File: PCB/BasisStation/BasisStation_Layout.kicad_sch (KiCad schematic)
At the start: 18 parts, among them J5 Conn_02x05_Odd_Even, J6 Conn_02x03_Odd_Even, U6 ESP32-S3-WROOM-1

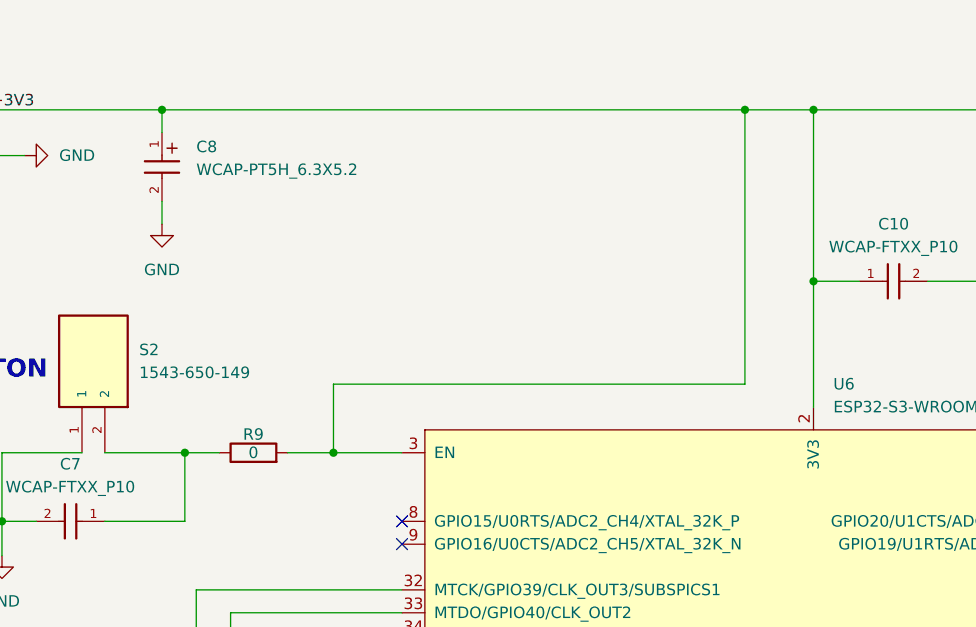
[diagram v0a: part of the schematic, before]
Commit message: Widerstand versetzt
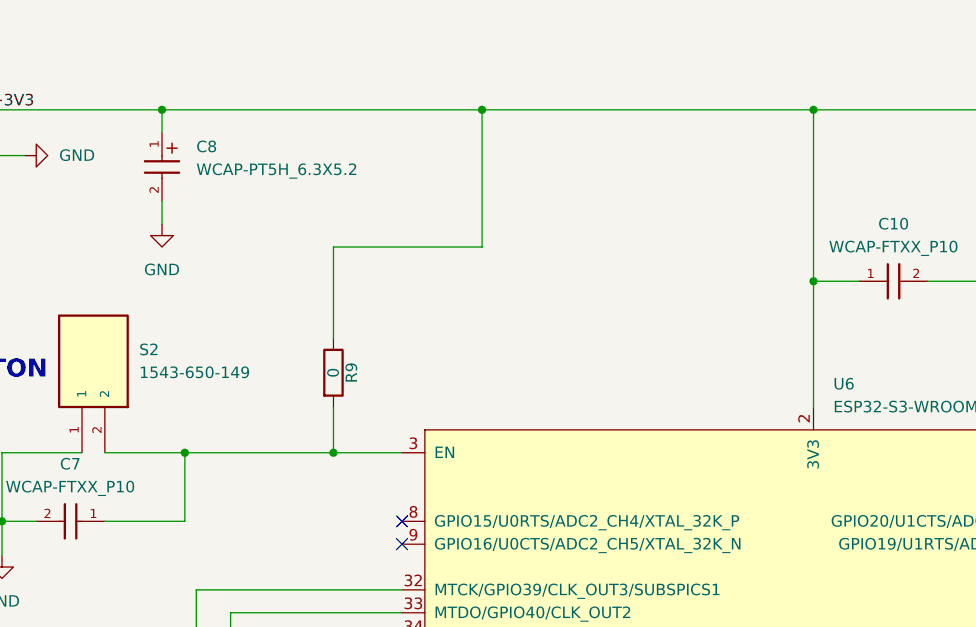
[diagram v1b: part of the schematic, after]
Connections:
- net +3V3: now also R9.1; no longer R9.2, U6.3 (EN)
- net at C7.1, S2.2: now also R9.2, U6.3 (EN); no longer R9.1
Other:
- moved on the sheet: R9

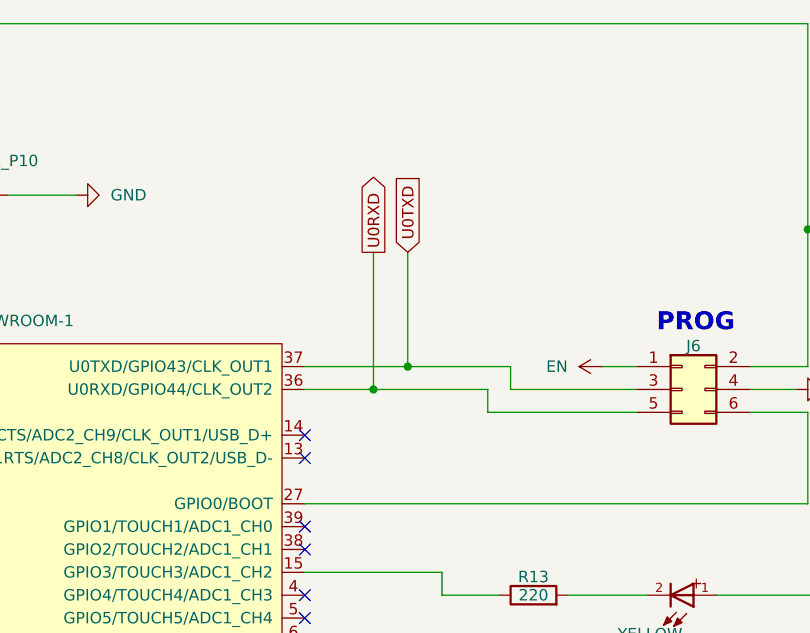
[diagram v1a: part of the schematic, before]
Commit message: USB-Bridge entfernt. Globale Bezeichner USB+ und USB- hinzugefügt
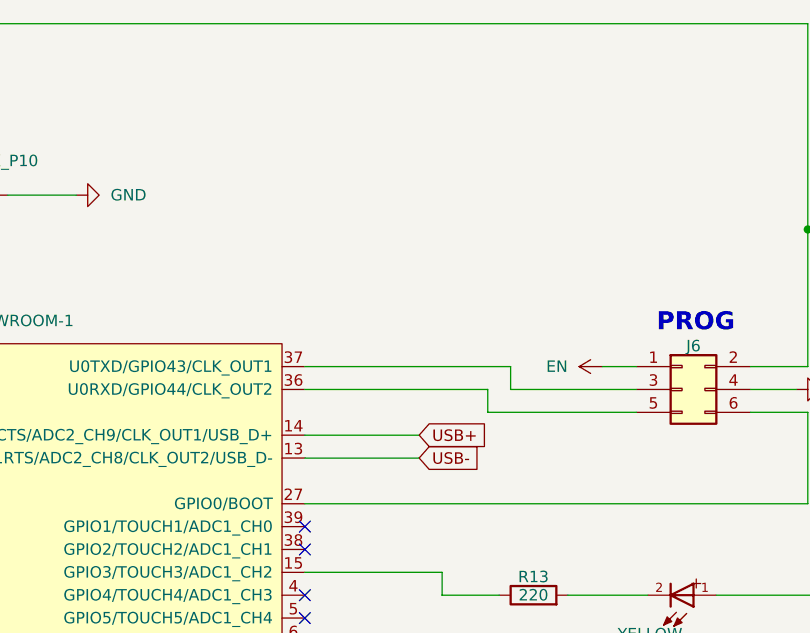
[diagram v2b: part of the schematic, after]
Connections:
- net USB-: now reaches U6.13 (GPIO19/U1RTS/ADC2_CH8/CLK_OUT2/USB_D-)
- net USB+: now reaches U6.14 (GPIO20/U1CTS/ADC2_CH9/CLK_OUT1/USB_D+)
- net U0RXD: no longer names the net of J6.5 (Pin_5), U6.36 (U0RXD/GPIO44/CLK_OUT2)
- net U0TXD: no longer names the net of J6.3 (Pin_3), U6.37 (U0TXD/GPIO43/CLK_OUT1)
- no-connect marks 26 -> 24
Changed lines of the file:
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@@
-	)
-	(junction
-		(at 195.58 60.96)
-		(diameter 0)
-		(color 0 0 0 0)
 	)
 	(junction
@@
 	)
 	(junction
-		(at 191.77 63.5)
-		(diameter 0)
-		(color 0 0 0 0)
-	)
-	(junction
 		(at 68.58 60.96)
 		(diameter 0)
@@
 	)
 	(no_connect
-		(at 184.15 68.58)
-	)
-	(no_connect
 		(at 92.71 127)
 	)
@@
 	)
 	(no_connect
-		(at 184.15 71.12)
-	)
-	(no_connect
 		(at 184.15 129.54)
 	)
@@
 	(wire
 		(pts
-			(xy 191.77 48.26) (xy 191.77 63.5)
-		)
-		(stroke
-			(width 0)
-			(type default)
-		)
-	)
-	(wire
-		(pts
 			(xy 48.26 68.58) (xy 52.07 68.58)
 		)
@@
 	(wire
 		(pts
-			(xy 195.58 48.26) (xy 195.58 60.96)
-		)
-		(stroke
-			(width 0)
-			(type default)
-		)
-	)
-	(wire
-		(pts
 			(xy 195.58 127) (xy 184.15 127)
 		)
@@
 	(wire
 		(pts
+			(xy 184.15 71.12) (xy 196.85 71.12)
+		)
+		(stroke
+			(width 0)
+			(type default)
+		)
+	)
+	(wire
+		(pts
 			(xy 213.36 104.14) (xy 222.25 104.14)
 		)
@@
 	(wire
 		(pts
-			(xy 191.77 63.5) (xy 204.47 63.5)
+			(xy 184.15 63.5) (xy 204.47 63.5)
 		)
 		(stroke
@@
 	(wire
 		(pts
+			(xy 184.15 68.58) (xy 196.85 68.58)
+		)
+		(stroke
+			(width 0)
+			(type default)
+		)
+	)
+	(wire
+		(pts
 			(xy 41.91 186.69) (xy 41.91 190.5)
 		)
@@
 	(wire
 		(pts
-			(xy 184.15 60.96) (xy 195.58 60.96)
+			(xy 184.15 60.96) (xy 207.01 60.96)
 		)
 		(stroke
@@
 	(wire
 		(pts
-			(xy 195.58 60.96) (xy 207.01 60.96)
-		)
-		(stroke
-			(width 0)
-			(type default)
-		)
-	)
-	(wire
-		(pts
 			(xy 68.58 68.58) (xy 68.58 60.96)
 		)
@@
 		(pts
 			(xy 199.39 83.82) (xy 184.15 83.82)
-		)
-		(stroke
-			(width 0)
-			(type default)
-		)
-	)
-	(wire
-		(pts
-			(xy 184.15 63.5) (xy 191.77 63.5)
 		)
 		(stroke
@@
 		)
 	)
-	(global_label "U0TXD"
+	(global_label "USB-"
 		(shape input)
-		(at 195.58 48.26 90)
+		(at 196.85 71.12 0)
 		(fields_autoplaced yes)
 		(effects
@@
 		)
 		(property "Intersheetrefs" "${INTERSHEET_REFS}"
-			(at 195.58 39.2877 90)
+			(at 205.2176 71.12 0)
 			(effects
 				(font
@@
 		)
 	)
-	(global_label "U0RXD"
-		(shape output)
-		(at 191.77 48.26 90)
+	(global_label "USB+"
+		(shape input)
+		(at 196.85 68.58 0)
 		(fields_autoplaced yes)
 		(effects
@@
 		)
 		(property "Intersheetrefs" "${INTERSHEET_REFS}"
-			(at 191.77 38.9853 90)
+			(at 205.2176 68.58 0)
 			(effects
 				(font

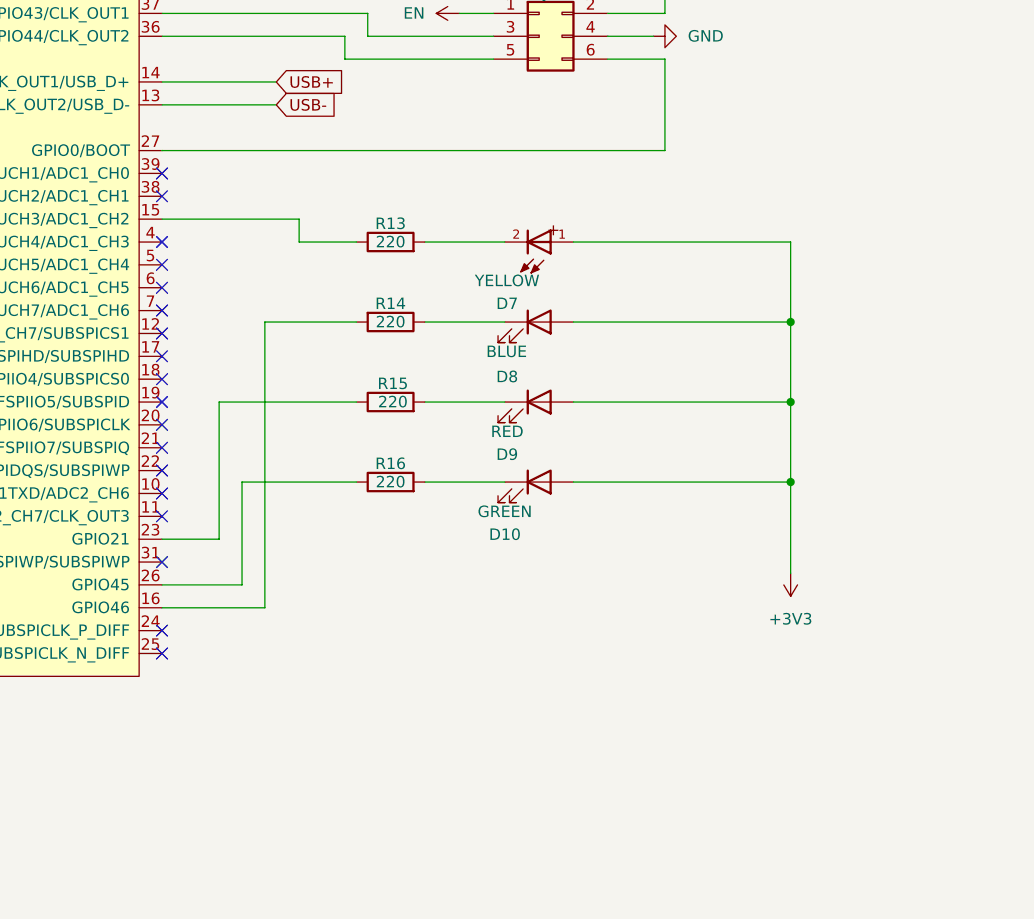
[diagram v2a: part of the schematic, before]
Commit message: Steuerund der LEDs umgebaut
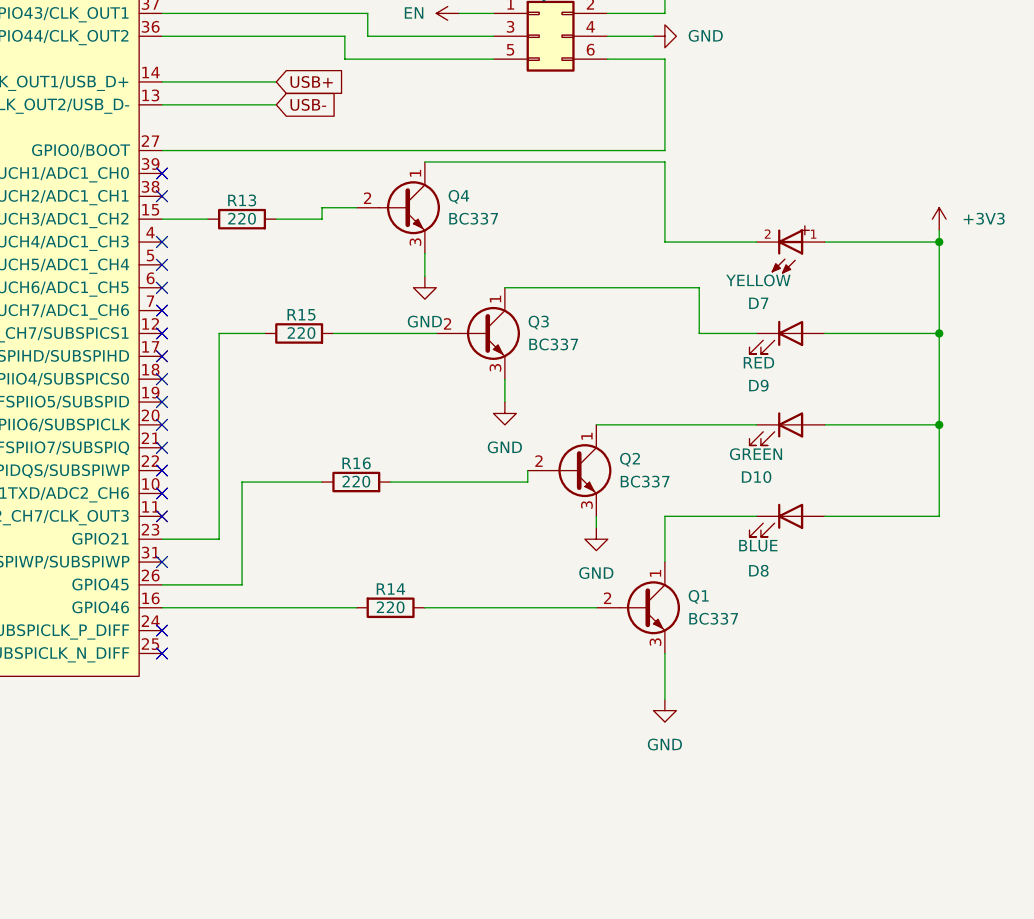
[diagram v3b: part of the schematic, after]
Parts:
- added Q1, Q2, Q3, Q4: BC337, Package_TO_SOT_THT:TO-92_Inline, symbol Transistor_BJT:BC337
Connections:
- net GND: now also Q1.3 (E), Q2.3 (E), Q3.3 (E), Q4.3 (E)
- net at D9.1 (K): now also Q3.1 (C); no longer R15.2
- net at D7.2: now also Q4.1 (C); no longer R13.2
- net at D8.1 (K): now also Q1.1 (C); no longer R14.1
- net at D10.1 (K): now also Q2.1 (C); no longer R16.2
- new net: Q1.2 (B), R14.1
- new net: Q4.2 (B), R13.2
- new net: Q3.2 (B), R15.2
- new net: Q2.2 (B), R16.2
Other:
- moved on the sheet: D10, D7, D8, D9, R13, R14, R15, R16

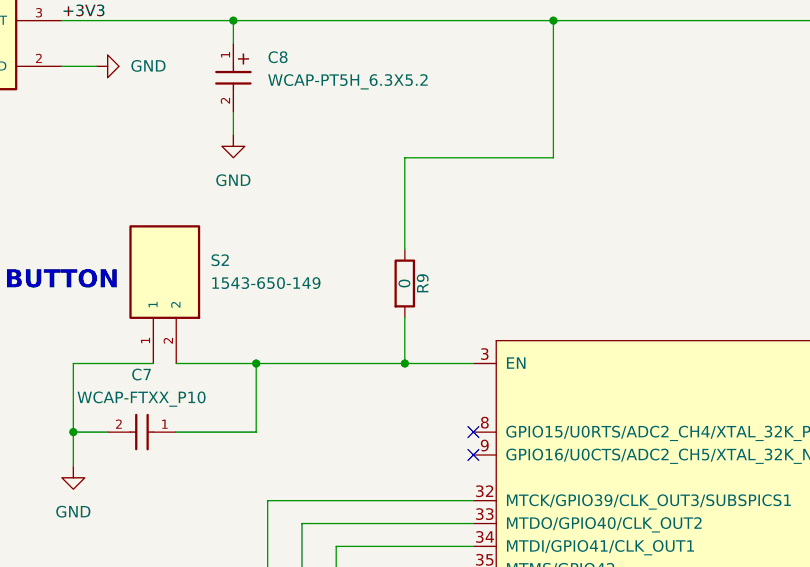
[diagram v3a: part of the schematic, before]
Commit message: Wert vom Widerstand angepasst
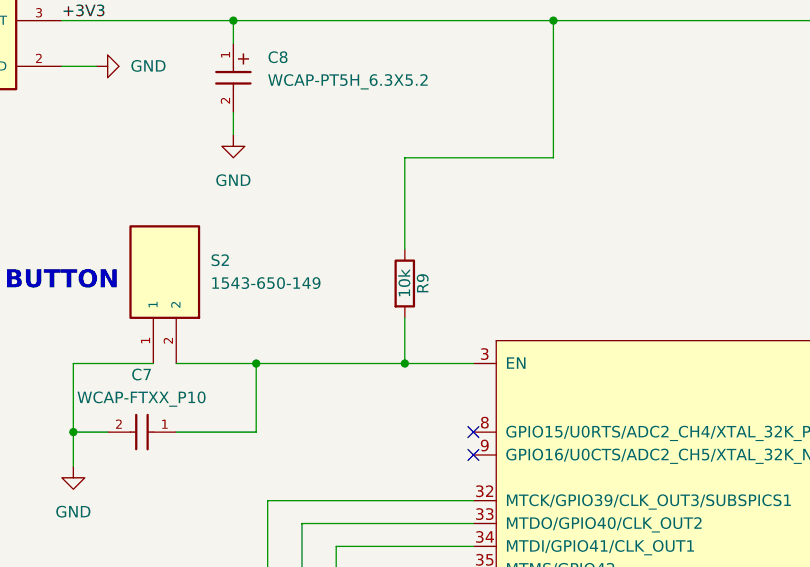
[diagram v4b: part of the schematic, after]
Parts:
- R9: value 0 -> 10k
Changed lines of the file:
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@@
 			)
 		)
-		(property "Value" "0"
+		(property "Value" "10k"
 			(at 85.09 52.07 90)
 			(effects

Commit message: widerstände umplaziert
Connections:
- net at Q1.1 (C): now also R14.2; no longer D8.1 (K)
- net at Q1.2 (B): now also U6.16 (GPIO46); no longer R14.1
- net at D9.1 (K): now also R15.2; no longer Q3.1 (C)
- net at D7.2: now also R13.2; no longer Q4.1 (C)
- net at Q4.2 (B): now also U6.15 (GPIO3/TOUCH3/ADC1_CH2); no longer R13.2
- net at R15.1: now also Q3.1 (C); no longer U6.23 (GPIO21)
- net at Q3.2 (B): now also U6.23 (GPIO21); no longer R15.2
- net at R13.1: now also Q4.1 (C); no longer U6.15 (GPIO3/TOUCH3/ADC1_CH2)
- net at D10.1 (K): now also R16.2; no longer Q2.1 (C)
- net at U6.26 (GPIO45): now also Q2.2 (B); no longer R16.1
- new net: D8.1 (K), R14.1
- new net: Q2.1 (C), R16.1
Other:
- moved on the sheet: R13, R14, R15, R16
